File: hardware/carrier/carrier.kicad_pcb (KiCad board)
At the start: 2 copper layers, 92 x 47 mm, 83 parts, among them J1 OBD pigtail, J2 GT-U7, J3 to Heltec JP2, J4 Heltec JP4, J5 Heltec JP5, Q1 2N7002, Q2 2N7002, Q3 AO3401A, Q4 AO3401A, Q5 HJ8205, U1 LMR36520ADDAR, U2 XC6206P332MR 3.3V, U3 TLV7022DDFR, U4 SN65HVD230DR, U5 DW01A, U6 TLV7022DDFR

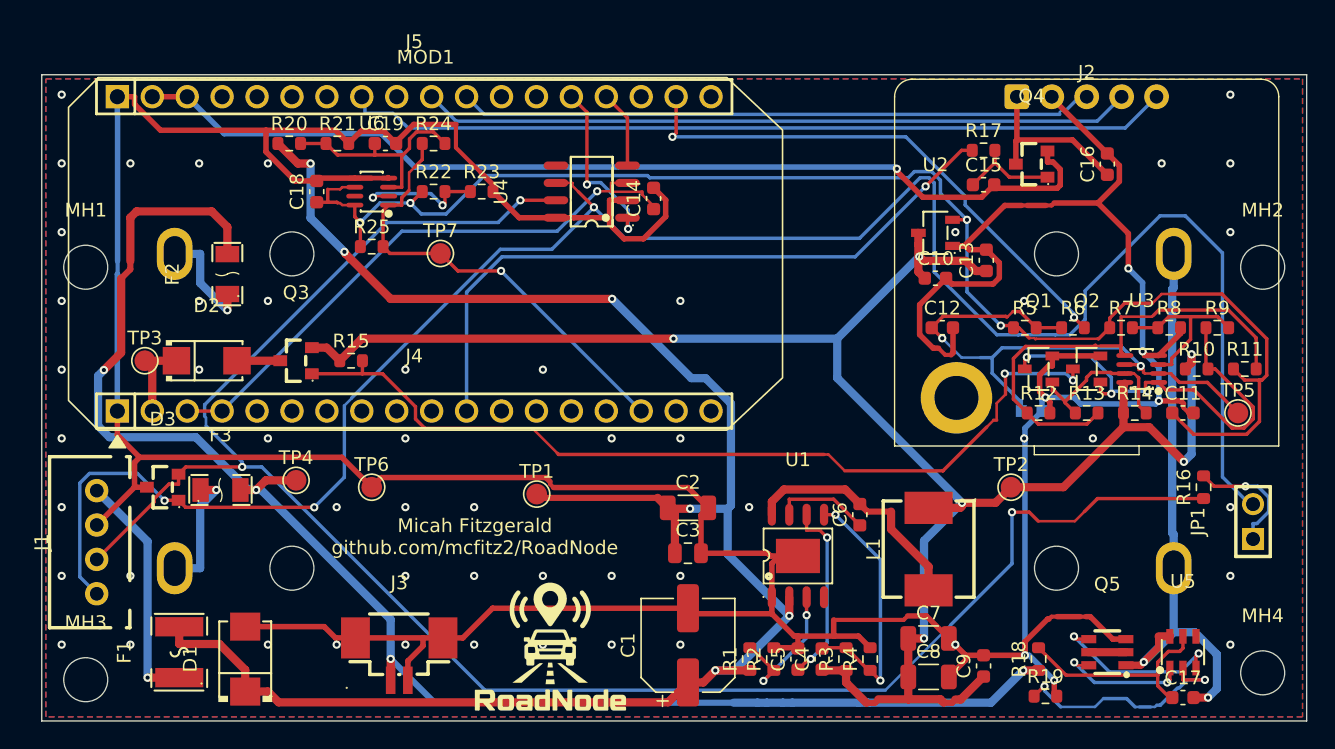
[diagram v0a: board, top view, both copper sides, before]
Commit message: Carrier: drop the battery, add a car-battery low-voltage cutoff
Remove the 18650 cells, DW01A/8205A protection, per-cell PTCs, NTC
charge gate and load switch. The node now runs only from the car.

- Always-on 3.3 V rail (HT7533 behind 10k + 24 V zener) and a REF3325
  2.5 V reference keep both comparators working with the buck off.
- TLV7022 half B is a low-voltage cutoff that pulls buck EN low via a
  2N7002: off below 11.6 V, on above 12.0 V nominal (worst case
  11.39-11.83 / 11.77-12.23 V), with a 6 s filter that rides through
  cranking. Clear of the measured 12.0 V key-on and 12.5 V resting
  voltages on the RAV4 and Maverick (sim/uvlo_thr.py).
- Wake comparator (half A) now references VREF: on 13.28 V, off
  12.96 V nominal (sim/wake_thr.py). Its tap is clamped to V3A with a
  1N4148WS so a load dump can't overdrive the comparator input.
- Board shrunk from 92x47 to 92x37 mm, still one-sided: low parts under
  the modules, tall parts in one strip; logo and credit on bottom silk.
- Remove the obsolete NTC sims.

Co-Authored-By: Claude Opus 5.5 <noreply@anthropic.com>
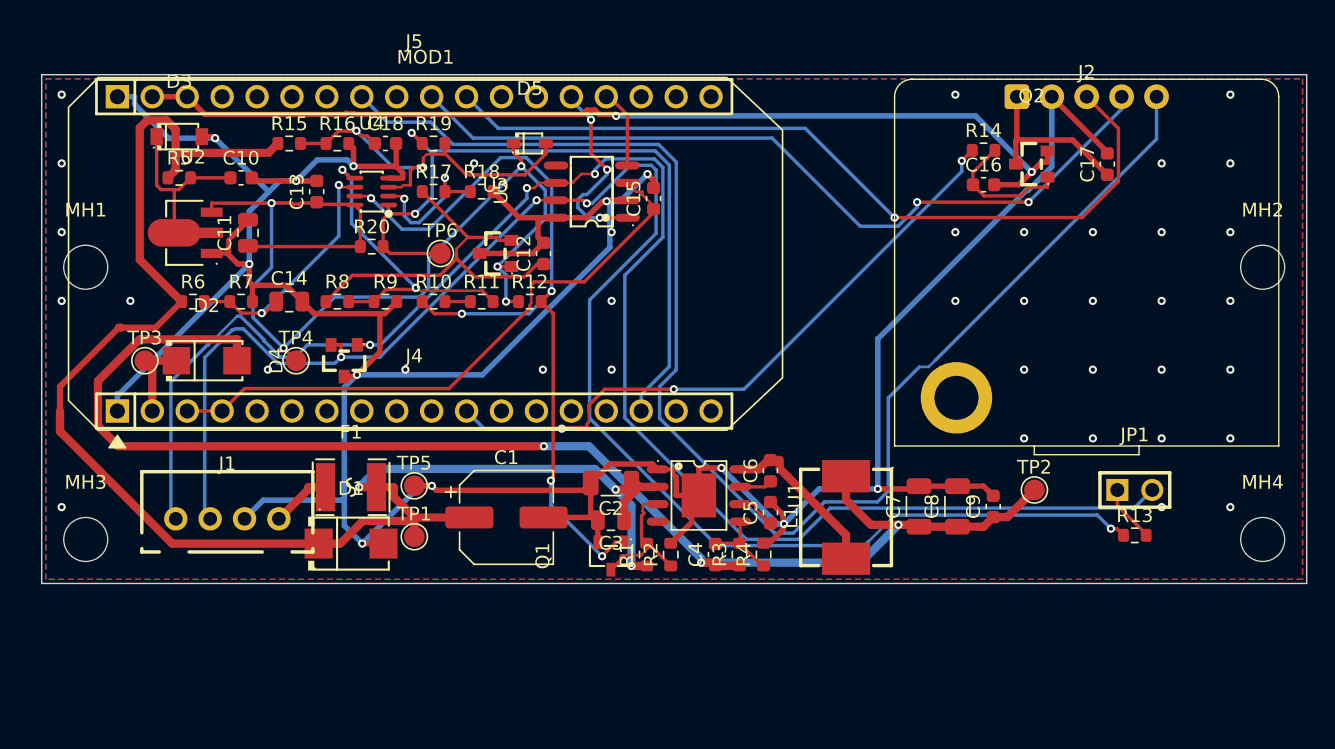
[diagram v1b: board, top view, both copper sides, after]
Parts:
- removed BT1, BT2: 18650, BH_18650_TH_P72.4
- removed C19: 100n, C_0603_1608Metric
- removed F2, F3: 2A hold, F1206
- removed J3: to Heltec JP2, CONN-SMD_P1.25-H_1.25T-2PWT
- removed Q3, Q4: AO3401A, SOT-23_L2.9-W1.3-P1.90-LS2.4-BR
- removed Q5: HJ8205, SOT-23-6_L2.9-W1.6-P0.95-LS2.8-BR
- removed R21: 220k, R_0603_1608Metric
- removed R22: 300k, R_0603_1608Metric
- removed R23: 750k, R_0603_1608Metric
- removed R24: 10M, R_0603_1608Metric
- removed R25: 1M, R_0603_1608Metric
- removed TH1: 100k B3950, R0603
- removed TP7: WAKE, TestPoint_Pad_D1.5mm
- removed U6: TLV7022DDFR, SOT-23-8_L2.9-W1.6-P0.65-LS2.8-BR
- added D4: PESD1CAN, SOT-23_L2.9-W1.3-P1.90-LS2.4-BR, F.Cu at (22.0, 20.8)
- added D5: 1N4148WS, SOD-323_L1.8-W1.3-LS2.5-RD, F.Cu at (35.5, 5.00)
- C11: value 1u -> 10u; footprint C_0603_1608Metric -> C_0805_2012Metric
- C14: value 100n -> 10u; footprint C_0603_1608Metric -> C_0805_2012Metric
- C15: value 10n -> 100n
- C16: value 1u -> 10n
- C17: value 100n -> 1u
- D3: value PESD1CAN -> BZT52C24; footprint SOT-23_L2.9-W1.3-P1.90-LS2.4-BR -> SOD-123_L2.7-W1.6-LS3.7-RD
- Q2: value 2N7002 -> AO3401A; footprint SOT-23-3_L2.9-W1.3-P1.90-LS2.4-BR -> SOT-23_L2.9-W1.3-P1.90-LS2.4-BR
- R10: value 1M -> 10M
- R11: value 470k -> 10M
- R12: value 220k -> 1M
- R13: value 10M -> 120
- R14: value 1M -> 10k
- R16: value 120 -> 220k
- R17: value 10k -> 47k
- R18: value 100 -> 750k
- R19: value 1k -> 10M
- R5: value 100k -> 10k
- R6: value 1k -> 3M
- R7: value 100k -> 750k
- R8: value 300k -> 510k
- R9: value 5.1M -> 10M
- TP4: value BATP -> V3A
- TP5: value NTC -> GND
- TP6: value GND -> WAKE
- U2: value XC6206P332MR 3.3V -> HT7533-1; footprint SOT-23-3_L2.9-W1.6-P1.90-LS2.8-BR -> SOT-89-3_L4.5-W2.5-P1.50-LS4.2-BR
- U3: value TLV7022DDFR -> REF3325 2.5V; footprint SOT-23-8_L2.9-W1.6-P0.65-LS2.8-BR -> SOT-23_L2.9-W1.3-P1.90-LS2.4-BR
- U4: value SN65HVD230DR -> TLV7022DDFR; footprint SOIC-8_L4.9-W3.9-P1.27-LS6.0-BL -> SOT-23-8_L2.9-W1.6-P0.65-LS2.8-BR
- U5: value DW01A -> SN65HVD230DR; footprint SOT-23-6_L2.9-W1.6-P0.95-LS2.8-BL -> SOIC-8_L4.9-W3.9-P1.27-LS6.0-BL
- moved C11 69.3 mm to (15.0, 11.5), turned to 90 degrees
- moved R16 67.8 mm to (21.5, 5.00), turned to 0 degrees
- moved R6 64.0 mm to (11.0, 16.5)
- moved R7 64.0 mm to (14.5, 16.5)
- moved R5 62.5 mm to (10.0, 7.50)
- moved R8 60.5 mm to (21.5, 16.5)
- moved R9 60.5 mm to (25.0, 16.5)
- moved TP5 60.1 mm to (27.1, 29.9)
- moved R19 60.0 mm to (28.5, 5.00)
- moved R10 55.7 mm to (28.5, 16.5)
- moved R11 55.7 mm to (32.0, 16.5)
- moved U5 54.5 mm to (40.0, 8.50), turned to 90 degrees
- moved U2 54.0 mm to (11.0, 11.5)
- moved R18 52.9 mm to (32.0, 8.50), turned to 0 degrees
- moved C10 51.0 mm to (14.5, 7.50)
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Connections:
- C10 pad 1: V5R -> V3A_IN
- C11 pad 1: V3REF -> V3A
- C12 pad 1: NTC_T -> VREF
- C13 pad 1: V5R -> V3A
- C14 pad 1: VEXT -> UV_TAP
- C15 pad 1: GNSS_G -> VEXT
- C15 pad 2: 3V3 -> GND
- C16 pad 1: GNSS_VCC -> GNSS_G
- C16 pad 2: GND -> 3V3
- C17 pad 1: PROT_VCC -> GNSS_VCC
- C17 pad 2: BAT_N -> GND
- C18 pad 1: V3REF -> V_TAP
- D2 pad 2: V5G -> V5R
- D3 pad 1: CANL -> V3A_IN
- D3 pad 2: CANH -> GND
- J5 pad 17: NTC_ADC -> (no net)
- Q1 pad 1: TOO_HOT -> UV_LOW
- Q1 pad 3: TEMP_OK -> EN
- Q2 pad 1: TEMP_OK -> GNSS_G
- Q2 pad 2: GND -> 3V3
- Q2 pad 3: CHG_GATE -> GNSS_VCC
- R10 pad 1: V5R -> UV_LOW
- R10 pad 2: TEMP_OK -> UV_HYS
- R11 pad 1: V3REF -> UV_HYS
- R11 pad 2: HB -> UV_REF
- R12 pad 1: HB -> V3A
- R12 pad 2: GND -> UV_LOW
- R13 pad 1: TOO_HOT -> CANH
- R13 pad 2: HB -> CAN_TERM
- R14 pad 1: V5R -> GNSS_EN_N
- R14 pad 2: TOO_HOT -> GNSS_G
- R15 pad 1: V5R -> VIN
- R15 pad 2: CHG_GATE -> V_TAP
- R16 pad 1: CANH -> V_TAP
- R16 pad 2: CAN_TERM -> GND
- R17 pad 1: GNSS_EN_N -> VREF
- R17 pad 2: GNSS_G -> WAKE_REF
- R18 pad 1: BAT_P -> WAKE_REF
- R18 pad 2: PROT_VCC -> GND
- R19 pad 1: PROT_VM -> CAR_ON
- R19 pad 2: GND -> V_TAP
- R20 pad 1: VIN -> V3A
- R20 pad 2: V_TAP -> CAR_ON
- R5 pad 1: V3REF -> VIN
- R5 pad 2: NTC_T -> V3A_IN
- R6 pad 1: NTC_T -> VIN
- R6 pad 2: NTC_ADC -> UV_TAP
- R7 pad 1: V3REF -> UV_TAP
- R7 pad 2: HA -> GND
- R8 pad 1: HA -> VREF
- R8 pad 2: GND -> UV_REF
- R9 pad 1: TEMP_OK -> UV_REF
- R9 pad 2: HA -> GND
- TP4 pad 1: BAT_P -> V3A
- TP5 pad 1: NTC_T -> GND
- TP6 pad 1: GND -> CAR_ON
- U2 pad 2: V3REF -> V3A_IN
- U2 pad 3: V5R -> V3A
- U3 pad 1: TEMP_OK -> V3A
- U3 pad 2: NTC_T -> VREF
- U3 pad 3: HA -> GND
- U4 pad 1: CAN_TX -> CAR_ON
- U4 pad 2: GND -> WAKE_REF
- U4 pad 3: VEXT -> V_TAP
- U4 pad 4: CAN_RX -> GND
- U4 pad 5: (no net) -> UV_REF
- U4 pad 6: CANL -> UV_TAP
- U4 pad 7: CANH -> UV_LOW
- U4 pad 8: GND -> V3A
- U5 pad 1: PROT_OD -> CAN_TX
- U5 pad 2: PROT_VM -> GND
- U5 pad 3: PROT_OC -> VEXT
- U5 pad 4: (no net) -> CAN_RX
- U5 pad 5: PROT_VCC -> (no net)
- U5 pad 6: BAT_N -> CANL
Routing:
- net BAT_P: track 111.1 -> 0.00 mm, vias 4 -> 0
- net V3REF: track 107.3 -> 0.00 mm, vias 4 -> 0
- net GND: track 344.6 -> 267.6 mm, vias 58 -> 49
- net V3A: track 0.00 -> 76.0 mm, vias 0 -> 5
- net CHG_GATE: track 65.4 -> 0.00 mm, vias 2 -> 0
- net UV_LOW: track 0.00 -> 60.2 mm, vias 0 -> 5
- net BAT_N: track 43.5 -> 0.00 mm, vias 2 -> 0
- net NTC_T: track 42.4 -> 0.00 mm, vias 2 -> 0
- net GPS_PPS: track 60.2 -> 102.5 mm
- net NTC_ADC: track 39.3 -> 0.00 mm, vias 2 -> 0
- net V5R: track 138.7 -> 100.1 mm, vias 6 -> 3
- net HB: track 34.5 -> 0.00 mm
- net TEMP_OK: track 31.6 -> 0.00 mm, vias 3 -> 0
- net VREF: track 0.00 -> 27.9 mm
- net CANL: track 145.3 -> 119.8 mm
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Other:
- board size 92 x 47 mm -> 92 x 37 mm
